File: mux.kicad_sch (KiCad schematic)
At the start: 7 parts, among them U11 MCP6001-OT, U12 DG9409EDN-T1-GE4

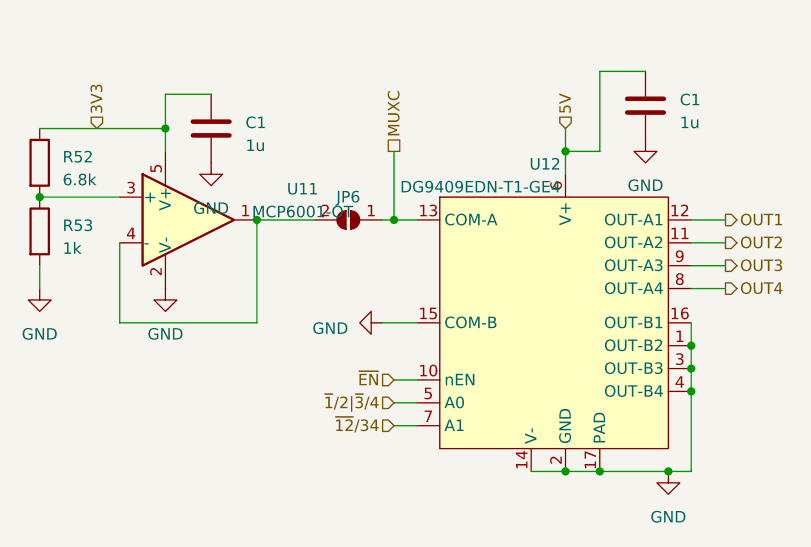
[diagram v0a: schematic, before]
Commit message: Build pogoplayground v1.0 - Fix continuity tester reference voltage - Fix SSR 5V supply
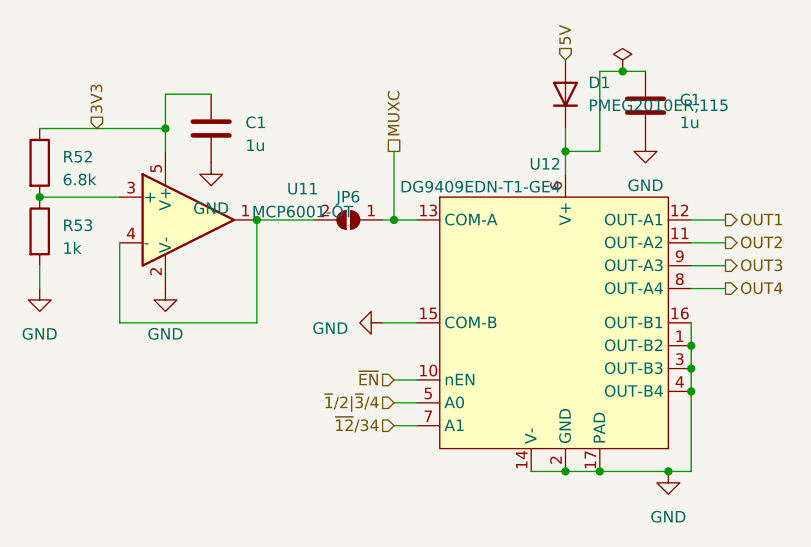
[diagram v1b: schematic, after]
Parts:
- added D1: PMEG2010ER,115, Diode_SMD:D_SOD-123, symbol Device:D
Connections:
- net 5V: now also D1.2 (A); no longer C1.1, U12.6 (V+)
- new net: C1.1, D1.1 (K), U12.6 (V+)
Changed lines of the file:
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@@
   (junction (at 134.62 82.55) (diameter 0) (color 0 0 0 0)
   )
+  (junction (at 160.02 66.04) (diameter 0) (color 0 0 0 0)
+  )
   (junction (at 165.1 110.49) (diameter 0) (color 0 0 0 0)
   )
@@
     (stroke (width 0) (type default))
   )
-  (wire (pts (xy 162.56 66.04) (xy 157.48 66.04))
+  (wire (pts (xy 162.56 66.04) (xy 160.02 66.04))
     (stroke (width 0) (type default))
   )
@@
   )
   (wire (pts (xy 157.48 74.93) (xy 153.67 74.93))
+    (stroke (width 0) (type default))
+  )
+  (wire (pts (xy 160.02 66.04) (xy 157.48 66.04))
     (stroke (width 0) (type default))
   )
@@
     (effects (font (size 1.27 1.27)) (justify right))
   )
-  (hierarchical_label "5V" (shape input) (at 153.67 72.39 90) (fields_autoplaced)
+  (hierarchical_label "5V" (shape input) (at 153.67 64.77 90) (fields_autoplaced)
     (effects (font (size 1.27 1.27)) (justify left))
   )
@@
     )
   )
+  (symbol (lib_id "power:PWR_FLAG") (at 160.02 66.04 0) (unit 1)
+    (in_bom yes) (on_board yes) (dnp no) (fields_autoplaced)
+    (property "Reference" "#FLG01" (at 160.02 64.135 0)
+      (effects (font (size 1.27 1.27)) hide)
+    )
+    (property "Value" "PWR_FLAG" (at 160.02 60.96 0)
+      (effects (font (size 1.27 1.27)) hide)
+    )
+    (property "Footprint" "" (at 160.02 66.04 0)
+      (effects (font (size 1.27 1.27)) hide)
+    )
+    (property "Datasheet" "~" (at 160.02 66.04 0)
+      (effects (font (size 1.27 1.27)) hide)
+    )
+    (pin "1")
+    (instances
+      (project "pogoplayground"
+        (path "/086fca78-0381-464b-8bbb-5a6257773e1c"
+          (reference "#FLG01") (unit 1)
+        )
+        (path "/086fca78-0381-464b-8bbb-5a6257773e1c/bf2a24e0-5659-4372-a698-9d9c10999d9c"
+          (reference "#FLG03") (unit 1)
+        )
+      )
+    )
+  )
   (symbol (lib_id "power:GND") (at 95.25 90.17 0) (unit 1)
     (in_bom yes) (on_board yes) (dnp no) (fields_autoplaced)
@@
         )
       )
+    )
+  )
+  (symbol (lib_id "Device:D") (at 153.67 68.58 90) (unit 1)
+    (in_bom yes) (on_board yes) (dnp no) (fields_autoplaced)
+    (property "Reference" "D1" (at 156.21 67.31 90)
+      (effects (font (size 1.27 1.27)) (justify right))
+    )
+    (property "Value" "PMEG2010ER,115" (at 156.21 69.85 90)
+      (effects (font (size 1.27 1.27)) (justify right))
+    )
+    (property "Footprint" "Diode_SMD:D_SOD-123" (at 153.67 68.58 0)
+      (effects (font (size 1.27 1.27)) hide)
+    )
+    (property "Datasheet" "~" (at 153.67 68.58 0)
+      (effects (font (size 1.27 1.27)) hide)
+    )
+    (property "Sim.Device" "D" (at 153.67 68.58 0)
+      (effects (font (size 1.27 1.27)) hide)
+    )
+    (property "Sim.Pins" "1=K 2=A" (at 153.67 68.58 0)
+      (effects (font (size 1.27 1.27)) hide)
+    )
+    (pin "1")
+    (pin "2")
+    (instances
+      (project "pogoplayground"
+        (path "/086fca78-0381-464b-8bbb-5a6257773e1c/bf2a24e0-5659-4372-a698-9d9c10999d9c"
+          (reference "D1") (unit 1)
+        )
+      )
